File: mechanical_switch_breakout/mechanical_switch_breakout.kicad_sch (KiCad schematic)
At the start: 4 parts, among them J1 Conn_01x04_Pin, SW1 SW_SPST, SW2 SW_SPST, SW3 SW_SPST

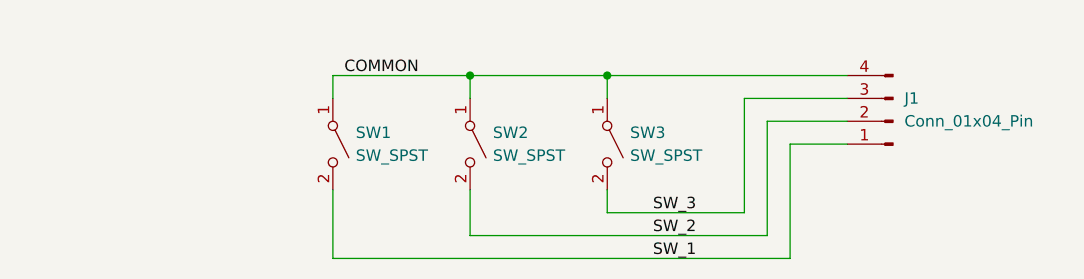
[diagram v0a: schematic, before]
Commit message: Added casing cad files
Designed a case in Onshape, made minor revisions to breakout boards.
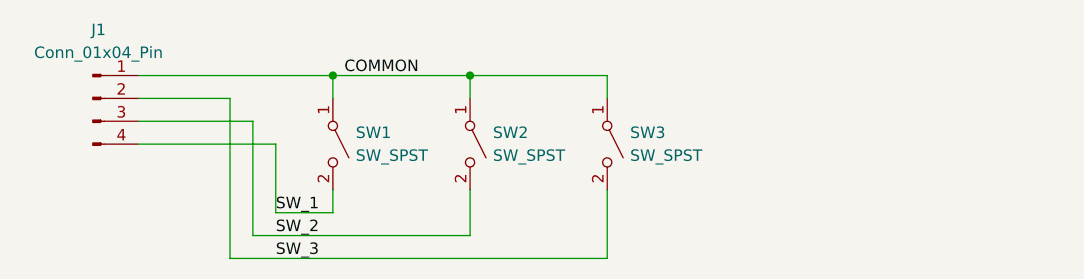
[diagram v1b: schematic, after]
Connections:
- net COMMON: now also J1.1 (Pin_1); no longer J1.4 (Pin_4)
- net SW_1: now also J1.4 (Pin_4); no longer J1.1 (Pin_1)
- net SW_2: now also J1.3 (Pin_3); no longer J1.2 (Pin_2)
- net SW_3: now also J1.2 (Pin_2); no longer J1.3 (Pin_3)
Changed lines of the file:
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@@
 		(title "Mechanical Switch Breakout Schematic")
 		(date "2024-06-07")
-		(rev "0.1.0")
+		(rev "0.1.1")
+	)
+	(junction
+		(at 78.74 54.61)
+		(diameter 0)
+		(color 0 0 0 0)
 	)
 	(junction
@@
 		(color 0 0 0 0)
 	)
-	(junction
-		(at 109.22 54.61)
-		(diameter 0)
-		(color 0 0 0 0)
-	)
-	(wire
-		(pts
-			(xy 129.54 74.93) (xy 129.54 62.23)
+	(wire
+		(pts
+			(xy 93.98 72.39) (xy 69.85 72.39)
 		)
 		(stroke
@@
 	(wire
 		(pts
-			(xy 109.22 54.61) (xy 135.89 54.61)
-		)
-		(stroke
-			(width 0)
-			(type default)
-		)
-	)
-	(wire
-		(pts
-			(xy 124.46 57.15) (xy 135.89 57.15)
-		)
-		(stroke
-			(width 0)
-			(type default)
-		)
-	)
-	(wire
-		(pts
-			(xy 78.74 67.31) (xy 78.74 74.93)
-		)
-		(stroke
-			(width 0)
-			(type default)
-		)
-	)
-	(wire
-		(pts
-			(xy 78.74 74.93) (xy 129.54 74.93)
+			(xy 109.22 74.93) (xy 67.31 74.93)
+		)
+		(stroke
+			(width 0)
+			(type default)
+		)
+	)
+	(wire
+		(pts
+			(xy 78.74 67.31) (xy 78.74 69.85)
+		)
+		(stroke
+			(width 0)
+			(type default)
+		)
+	)
+	(wire
+		(pts
+			(xy 69.85 72.39) (xy 69.85 59.69)
 		)
 		(stroke
@@
 	(wire
 		(pts
-			(xy 129.54 62.23) (xy 135.89 62.23)
-		)
-		(stroke
-			(width 0)
-			(type default)
-		)
-	)
-	(wire
-		(pts
 			(xy 93.98 54.61) (xy 93.98 57.15)
 		)
@@
 	(wire
 		(pts
+			(xy 67.31 57.15) (xy 57.15 57.15)
+		)
+		(stroke
+			(width 0)
+			(type default)
+		)
+	)
+	(wire
+		(pts
+			(xy 67.31 57.15) (xy 67.31 74.93)
+		)
+		(stroke
+			(width 0)
+			(type default)
+		)
+	)
+	(wire
+		(pts
 			(xy 78.74 54.61) (xy 78.74 57.15)
 		)
@@
 	(wire
 		(pts
-			(xy 109.22 67.31) (xy 109.22 69.85)
+			(xy 78.74 69.85) (xy 72.39 69.85)
+		)
+		(stroke
+			(width 0)
+			(type default)
+		)
+	)
+	(wire
+		(pts
+			(xy 109.22 67.31) (xy 109.22 74.93)
 		)
 		(stroke
@@
 	(wire
 		(pts
-			(xy 109.22 69.85) (xy 124.46 69.85)
-		)
-		(stroke
-			(width 0)
-			(type default)
-		)
-	)
-	(wire
-		(pts
-			(xy 127 59.69) (xy 135.89 59.69)
-		)
-		(stroke
-			(width 0)
-			(type default)
-		)
-	)
-	(wire
-		(pts
-			(xy 124.46 57.15) (xy 124.46 69.85)
-		)
-		(stroke
-			(width 0)
-			(type default)
-		)
-	)
-	(wire
-		(pts
-			(xy 127 72.39) (xy 127 59.69)
+			(xy 57.15 62.23) (xy 72.39 62.23)
+		)
+		(stroke
+			(width 0)
+			(type default)
+		)
+	)
+	(wire
+		(pts
+			(xy 57.15 54.61) (xy 78.74 54.61)
+		)
+		(stroke
+			(width 0)
+			(type default)
+		)
+	)
+	(wire
+		(pts
+			(xy 57.15 59.69) (xy 69.85 59.69)
 		)
 		(stroke
@@
 	(wire
 		(pts
-			(xy 93.98 72.39) (xy 127 72.39)
-		)
-		(stroke
-			(width 0)
-			(type default)
-		)
-	)
-	(label "SW_2"
-		(at 114.3 72.39 0)
+			(xy 72.39 69.85) (xy 72.39 62.23)
+		)
+		(stroke
+			(width 0)
+			(type default)
+		)
+	)
+	(label "SW_3"
+		(at 72.39 74.93 0)
 		(fields_autoplaced yes)
 		(effects
@@
 	)
 	(label "SW_1"
-		(at 114.3 74.93 0)
+		(at 72.39 69.85 0)
 		(fields_autoplaced yes)
 		(effects
@@
 		)
 	)
-	(label "SW_3"
-		(at 114.3 69.85 0)
+	(label "SW_2"
+		(at 72.39 72.39 0)
 		(fields_autoplaced yes)
 		(effects
@@
 	)
 	(symbol
-		(lib_id "Connector:Conn_01x04_Pin")
-		(at 140.97 59.69 180)
-		(unit 1)
-		(exclude_from_sim no)
-		(in_bom yes)
-		(on_board yes)
-		(dnp no)
-		(fields_autoplaced yes)
-		(property "Reference" "J1"
-			(at 142.24 57.1499 0)
-			(effects
-				(font
-					(size 1.27 1.27)
-				)
-				(justify right)
-			)
-		)
-		(property "Value" "Conn_01x04_Pin"
-			(at 142.24 59.6899 0)
-			(effects
-				(font
-					(size 1.27 1.27)
-				)
-				(justify right)
-			)
-		)
-		(property "Footprint" "Connector_PinHeader_2.54mm:PinHeader_1x04_P2.54mm_Horizontal"
-			(at 140.97 59.69 0)
-			(effects
-				(font
-					(size 1.27 1.27)
-				)
-				(hide yes)
-			)
-		)
-		(property "Datasheet" "~"
-			(at 140.97 59.69 0)
-			(effects
-				(font
-					(size 1.27 1.27)
-				)
-				(hide yes)
-			)
-		)
-		(property "Description" "Generic connector, single row, 01x04, script generated"
-			(at 140.97 59.69 0)
-			(effects
-				(font
-					(size 1.27 1.27)
-				)
-				(hide yes)
-			)
-		)
-		(pin "1"
-		)
-		(pin "2"
-		)
-		(pin "3"
-		)
-		(pin "4"
-		)
-		(instances
-			(project "mechanical_switch_breakout"
-				(path "/8d0d4ecb-3b5a-4c86-b69f-39339f1c9cc5"
-					(reference "J1")
-					(unit 1)
-				)
-			)
-		)
-	)
-	(symbol
 		(lib_id "Switch:SW_SPST")
 		(at 109.22 62.23 270)
@@
 					(unit 1)
 				)
+			)
+		)
+	)
+	(symbol
+		(lib_id "Connector:Conn_01x04_Pin")
+		(at 52.07 57.15 0)
+		(unit 1)
+		(exclude_from_sim no)
+		(in_bom yes)
+		(on_board yes)
+		(dnp no)
+		(fields_autoplaced yes)
+		(property "Reference" "J1"
+			(at 52.705 49.53 0)
+			(effects
+				(font
+					(size 1.27 1.27)
+				)
+			)
+		)
+		(property "Value" "Conn_01x04_Pin"
+			(at 52.705 52.07 0)
+			(effects
+				(font
+					(size 1.27 1.27)
+				)
+			)
+		)
+		(property "Footprint" "Connector_PinHeader_2.54mm:PinHeader_1x04_P2.54mm_Horizontal"
+			(at 52.07 57.15 0)
+			(effects
+				(font
+					(size 1.27 1.27)
+				)
+				(hide yes)
+			)
+		)
+		(property "Datasheet" "~"
+			(at 52.07 57.15 0)
+			(effects
+				(font
+					(size 1.27 1.27)
+				)
+				(hide yes)
+			)
+		)
+		(property "Description" "Generic connector, single row, 01x04, script generated"
+			(at 52.07 57.15 0)
+			(effects
+				(font
+					(size 1.27 1.27)
+				)
+				(hide yes)
+			)
+		)
+		(pin "1"
+		)
+		(pin "2"
+		)
+		(pin "3"
+		)
+		(pin "4"
+		)
+		(instances
+			(project "mechanical_switch_breakout"
+				(path "/8d0d4ecb-3b5a-4c86-b69f-39339f1c9cc5"
+					(reference "J1")
+					(unit 1)
+				)
